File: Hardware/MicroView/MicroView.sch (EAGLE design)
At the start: 23 parts, among them J1 OLED_SCREEN, J2 MICROVIEW-16, J3 M03NS_SLIM, U1 MIC5205 3.3V, U2 SPX3819M5-L-5-0, U3 ATMEGA328P, Y1 16MHz

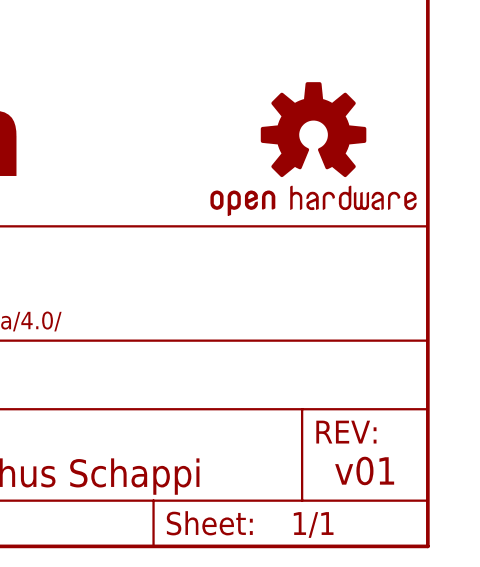
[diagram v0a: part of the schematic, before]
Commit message: Adding fids to both boards
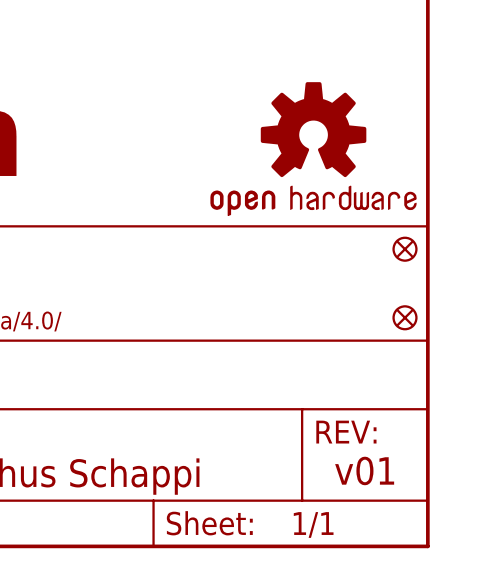
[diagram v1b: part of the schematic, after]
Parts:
- added FID1, FID3: FIDUCIAL1X2, SparkFun-Aesthetics:FIDUCIAL1X2
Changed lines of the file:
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@@
 <grid distance="0.1" unitdist="inch" unit="inch" style="lines" multiple="1" display="no" altdistance="0.01" altunitdist="inch" altunit="inch"/>
 <layers>
-<layer number="1" name="Top" color="4" fill="1" visible="no" active="no"/>
-<layer number="2" name="Route2" color="1" fill="3" visible="no" active="no"/>
-<layer number="3" name="Route3" color="4" fill="3" visible="no" active="no"/>
-<layer number="4" name="Route4" color="1" fill="4" visible="no" active="no"/>
-<layer number="5" name="Route5" color="4" fill="4" visible="no" active="no"/>
-<layer number="6" name="Route6" color="1" fill="8" visible="no" active="no"/>
-<layer number="7" name="Route7" color="4" fill="8" visible="no" active="no"/>
-<layer number="8" name="Route8" color="1" fill="2" visible="no" active="no"/>
-<layer number="9" name="Route9" color="4" fill="2" visible="no" active="no"/>
-<layer number="10" name="Route10" color="1" fill="7" visible="no" active="no"/>
-<layer number="11" name="Route11" color="4" fill="7" visible="no" active="no"/>
-<layer number="12" name="Route12" color="1" fill="5" visible="no" active="no"/>
-<layer number="13" name="Route13" color="4" fill="5" visible="no" active="no"/>
-<layer number="14" name="Route14" color="1" fill="6" visible="no" active="no"/>
-<layer number="15" name="Route15" color="4" fill="6" visible="no" active="no"/>
-<layer number="16" name="Bottom" color="1" fill="1" visible="no" active="no"/>
-<layer number="17" name="Pads" color="2" fill="1" visible="no" active="no"/>
-<layer number="18" name="Vias" color="2" fill="1" visible="no" active="no"/>
-<layer number="19" name="Unrouted" color="6" fill="1" visible="no" active="no"/>
-<layer number="20" name="Dimension" color="15" fill="1" visible="no" active="no"/>
-<layer number="21" name="tPlace" color="16" fill="1" visible="no" active="no"/>
-<layer number="22" name="bPlace" color="14" fill="1" visible="no" active="no"/>
-<layer number="23" name="tOrigins" color="15" fill="1" visible="no" active="no"/>
-<layer number="24" name="bOrigins" color="15" fill="1" visible="no" active="no"/>
-<layer number="25" name="tNames" color="7" fill="1" visible="no" active="no"/>
-<layer number="26" name="bNames" color="7" fill="1" visible="no" active="no"/>
-<layer number="27" name="tValues" color="7" fill="1" visible="no" active="no"/>
-<layer number="28" name="bValues" color="7" fill="1" visible="no" active="no"/>
+<layer number="1" name="Top" color="4" fill="1" visible="yes" active="no"/>
+<layer number="2" name="Route2" color="1" fill="3" visible="yes" active="no"/>
+<layer number="3" name="Route3" color="4" fill="3" visible="yes" active="no"/>
+<layer number="4" name="Route4" color="1" fill="4" visible="yes" active="no"/>
+<layer number="5" name="Route5" color="4" fill="4" visible="yes" active="no"/>
+<layer number="6" name="Route6" color="1" fill="8" visible="yes" active="no"/>
+<layer number="7" name="Route7" color="4" fill="8" visible="yes" active="no"/>
+<layer number="8" name="Route8" color="1" fill="2" visible="yes" active="no"/>
+<layer number="9" name="Route9" color="4" fill="2" visible="yes" active="no"/>
+<layer number="10" name="Route10" color="1" fill="7" visible="yes" active="no"/>
+<layer number="11" name="Route11" color="4" fill="7" visible="yes" active="no"/>
+<layer number="12" name="Route12" color="1" fill="5" visible="yes" active="no"/>
+<layer number="13" name="Route13" color="4" fill="5" visible="yes" active="no"/>
+<layer number="14" name="Route14" color="1" fill="6" visible="yes" active="no"/>
+<layer number="15" name="Route15" color="4" fill="6" visible="yes" active="no"/>
+<layer number="16" name="Bottom" color="1" fill="1" visible="yes" active="no"/>
+<layer number="17" name="Pads" color="2" fill="1" visible="yes" active="no"/>
+<layer number="18" name="Vias" color="2" fill="1" visible="yes" active="no"/>
+<layer number="19" name="Unrouted" color="6" fill="1" visible="yes" active="no"/>
+<layer number="20" name="Dimension" color="15" fill="1" visible="yes" active="no"/>
+<layer number="21" name="tPlace" color="16" fill="1" visible="yes" active="no"/>
+<layer number="22" name="bPlace" color="14" fill="1" visible="yes" active="no"/>
+<layer number="23" name="tOrigins" color="15" fill="1" visible="yes" active="no"/>
+<layer number="24" name="bOrigins" color="15" fill="1" visible="yes" active="no"/>
+<layer number="25" name="tNames" color="7" fill="1" visible="yes" active="no"/>
+<layer number="26" name="bNames" color="7" fill="1" visible="yes" active="no"/>
+<layer number="27" name="tValues" color="7" fill="1" visible="yes" active="no"/>
+<layer number="28" name="bValues" color="7" fill="1" visible="yes" active="no"/>
 <layer number="29" name="tStop" color="7" fill="3" visible="no" active="no"/>
 <layer number="30" name="bStop" color="7" fill="6" visible="no" active="no"/>
@@
 <layer number="35" name="tGlue" color="7" fill="4" visible="no" active="no"/>
 <layer number="36" name="bGlue" color="7" fill="5" visible="no" active="no"/>
-<layer number="37" name="tTest" color="7" fill="1" visible="no" active="no"/>
-<layer number="38" name="bTest" color="7" fill="1" visible="no" active="no"/>
+<layer number="37" name="tTest" color="7" fill="1" visible="yes" active="no"/>
+<layer number="38" name="bTest" color="7" fill="1" visible="yes" active="no"/>
 <layer number="39" name="tKeepout" color="4" fill="11" visible="no" active="no"/>
 <layer number="40" name="bKeepout" color="1" fill="11" visible="no" active="no"/>
@@
 <layer number="44" name="Drills" color="7" fill="1" visible="no" active="no"/>
 <layer number="45" name="Holes" color="7" fill="1" visible="no" active="no"/>
-<layer number="46" name="Milling" color="3" fill="1" visible="no" active="no"/>
-<layer number="47" name="Measures" color="7" fill="1" visible="no" active="no"/>
-<layer number="48" name="Document" color="7" fill="1" visible="no" active="no"/>
-<layer number="49" name="Reference" color="7" fill="1" visible="no" active="no"/>
-<layer number="50" name="dxf" color="7" fill="1" visible="no" active="no"/>
-<layer number="51" name="tDocu" color="6" fill="1" visible="no" active="no"/>
-<layer number="52" name="bDocu" color="7" fill="1" visible="no" active="no"/>
-<layer number="53" name="tGND_GNDA" color="7" fill="9" visible="no" active="no"/>
-<layer number="54" name="bGND_GNDA" color="1" fill="9" visible="no" active="no"/>
-<layer number="56" name="wert" color="7" fill="1" visible="no" active="no"/>
+<layer number="46" name="Milling" color="3" fill="1" visible="yes" active="no"/>
+<layer number="47" name="Measures" color="7" fill="1" visible="yes" active="no"/>
+<layer number="48" name="Document" color="7" fill="1" visible="yes" active="no"/>
+<layer number="49" name="Reference" color="7" fill="1" visible="yes" active="no"/>
+<layer number="50" name="dxf" color="7" fill="1" visible="yes" active="no"/>
+<layer number="51" name="tDocu" color="6" fill="1" visible="yes" active="no"/>
+<layer number="52" name="bDocu" color="7" fill="1" visible="yes" active="no"/>
+<layer number="53" name="tGND_GNDA" color="7" fill="9" visible="yes" active="no"/>
+<layer number="54" name="bGND_GNDA" color="1" fill="9" visible="yes" active="no"/>
+<layer number="56" name="wert" color="7" fill="1" visible="yes" active="no"/>
 <layer number="91" name="Nets" color="2" fill="1" visible="yes" active="yes"/>
 <layer number="92" name="Busses" color="1" fill="1" visible="yes" active="yes"/>
@@
 <part name="LOGO1" library="SparkFun-Aesthetics" deviceset="OSHW-LOGO" device="S"/>
 <part name="LOGO4" library="SparkFun-Aesthetics" deviceset="SFE_LOGO_NAME_FLAME" device=".1_INCH"/>
+<part name="FID1" library="SparkFun-Aesthetics" deviceset="FIDUCIAL" device="1X2" value="FIDUCIAL1X2"/>
+<part name="FID3" library="SparkFun-Aesthetics" deviceset="FIDUCIAL" device="1X2"/>
 </parts>
 <sheets>
@@
 <instance part="LOGO1" gate="G$1" x="236.22" y="45.72"/>
 <instance part="LOGO4" gate="G$1" x="148.082" y="36.576"/>
+<instance part="FID1" gate="G$1" x="246.38" y="33.02"/>
+<instance part="FID3" gate="G$1" x="246.38" y="25.4"/>
 </instances>
 <busses>

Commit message: Staggering/increasing drill on headers
Also spacing out resistors, increasing header fp on MicroViewUSB.
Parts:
- FID1, FID3: value FIDUCIAL1X2 -> FIDUCIALUFIDUCIAL; device SparkFun-Aesthetics:FIDUCIAL1X2 -> SparkFun-Aesthetics:FIDUCIALUFIDUCIAL
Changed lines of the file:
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@@
 <grid distance="0.1" unitdist="inch" unit="inch" style="lines" multiple="1" display="no" altdistance="0.01" altunitdist="inch" altunit="inch"/>
 <layers>
-<layer number="1" name="Top" color="4" fill="1" visible="yes" active="no"/>
-<layer number="2" name="Route2" color="1" fill="3" visible="yes" active="no"/>
-<layer number="3" name="Route3" color="4" fill="3" visible="yes" active="no"/>
-<layer number="4" name="Route4" color="1" fill="4" visible="yes" active="no"/>
-<layer number="5" name="Route5" color="4" fill="4" visible="yes" active="no"/>
-<layer number="6" name="Route6" color="1" fill="8" visible="yes" active="no"/>
-<layer number="7" name="Route7" color="4" fill="8" visible="yes" active="no"/>
-<layer number="8" name="Route8" color="1" fill="2" visible="yes" active="no"/>
-<layer number="9" name="Route9" color="4" fill="2" visible="yes" active="no"/>
-<layer number="10" name="Route10" color="1" fill="7" visible="yes" active="no"/>
-<layer number="11" name="Route11" color="4" fill="7" visible="yes" active="no"/>
-<layer number="12" name="Route12" color="1" fill="5" visible="yes" active="no"/>
-<layer number="13" name="Route13" color="4" fill="5" visible="yes" active="no"/>
-<layer number="14" name="Route14" color="1" fill="6" visible="yes" active="no"/>
-<layer number="15" name="Route15" color="4" fill="6" visible="yes" active="no"/>
-<layer number="16" name="Bottom" color="1" fill="1" visible="yes" active="no"/>
-<layer number="17" name="Pads" color="2" fill="1" visible="yes" active="no"/>
-<layer number="18" name="Vias" color="2" fill="1" visible="yes" active="no"/>
-<layer number="19" name="Unrouted" color="6" fill="1" visible="yes" active="no"/>
-<layer number="20" name="Dimension" color="15" fill="1" visible="yes" active="no"/>
-<layer number="21" name="tPlace" color="16" fill="1" visible="yes" active="no"/>
-<layer number="22" name="bPlace" color="14" fill="1" visible="yes" active="no"/>
-<layer number="23" name="tOrigins" color="15" fill="1" visible="yes" active="no"/>
-<layer number="24" name="bOrigins" color="15" fill="1" visible="yes" active="no"/>
-<layer number="25" name="tNames" color="7" fill="1" visible="yes" active="no"/>
-<layer number="26" name="bNames" color="7" fill="1" visible="yes" active="no"/>
-<layer number="27" name="tValues" color="7" fill="1" visible="yes" active="no"/>
-<layer number="28" name="bValues" color="7" fill="1" visible="yes" active="no"/>
+<layer number="1" name="Top" color="4" fill="1" visible="no" active="no"/>
+<layer number="2" name="Route2" color="1" fill="3" visible="no" active="no"/>
+<layer number="3" name="Route3" color="4" fill="3" visible="no" active="no"/>
+<layer number="4" name="Route4" color="1" fill="4" visible="no" active="no"/>
+<layer number="5" name="Route5" color="4" fill="4" visible="no" active="no"/>
+<layer number="6" name="Route6" color="1" fill="8" visible="no" active="no"/>
+<layer number="7" name="Route7" color="4" fill="8" visible="no" active="no"/>
+<layer number="8" name="Route8" color="1" fill="2" visible="no" active="no"/>
+<layer number="9" name="Route9" color="4" fill="2" visible="no" active="no"/>
+<layer number="10" name="Route10" color="1" fill="7" visible="no" active="no"/>
+<layer number="11" name="Route11" color="4" fill="7" visible="no" active="no"/>
+<layer number="12" name="Route12" color="1" fill="5" visible="no" active="no"/>
+<layer number="13" name="Route13" color="4" fill="5" visible="no" active="no"/>
+<layer number="14" name="Route14" color="1" fill="6" visible="no" active="no"/>
+<layer number="15" name="Route15" color="4" fill="6" visible="no" active="no"/>
+<layer number="16" name="Bottom" color="1" fill="1" visible="no" active="no"/>
+<layer number="17" name="Pads" color="2" fill="1" visible="no" active="no"/>
+<layer number="18" name="Vias" color="2" fill="1" visible="no" active="no"/>
+<layer number="19" name="Unrouted" color="6" fill="1" visible="no" active="no"/>
+<layer number="20" name="Dimension" color="15" fill="1" visible="no" active="no"/>
+<layer number="21" name="tPlace" color="16" fill="1" visible="no" active="no"/>
+<layer number="22" name="bPlace" color="14" fill="1" visible="no" active="no"/>
+<layer number="23" name="tOrigins" color="15" fill="1" visible="no" active="no"/>
+<layer number="24" name="bOrigins" color="15" fill="1" visible="no" active="no"/>
+<layer number="25" name="tNames" color="7" fill="1" visible="no" active="no"/>
+<layer number="26" name="bNames" color="7" fill="1" visible="no" active="no"/>
+<layer number="27" name="tValues" color="7" fill="1" visible="no" active="no"/>
+<layer number="28" name="bValues" color="7" fill="1" visible="no" active="no"/>
 <layer number="29" name="tStop" color="7" fill="3" visible="no" active="no"/>
 <layer number="30" name="bStop" color="7" fill="6" visible="no" active="no"/>
@@
 <layer number="35" name="tGlue" color="7" fill="4" visible="no" active="no"/>
 <layer number="36" name="bGlue" color="7" fill="5" visible="no" active="no"/>
-<layer number="37" name="tTest" color="7" fill="1" visible="yes" active="no"/>
-<layer number="38" name="bTest" color="7" fill="1" visible="yes" active="no"/>
+<layer number="37" name="tTest" color="7" fill="1" visible="no" active="no"/>
+<layer number="38" name="bTest" color="7" fill="1" visible="no" active="no"/>
 <layer number="39" name="tKeepout" color="4" fill="11" visible="no" active="no"/>
 <layer number="40" name="bKeepout" color="1" fill="11" visible="no" active="no"/>
@@
 <layer number="44" name="Drills" color="7" fill="1" visible="no" active="no"/>
 <layer number="45" name="Holes" color="7" fill="1" visible="no" active="no"/>
-<layer number="46" name="Milling" color="3" fill="1" visible="yes" active="no"/>
-<layer number="47" name="Measures" color="7" fill="1" visible="yes" active="no"/>
-<layer number="48" name="Document" color="7" fill="1" visible="yes" active="no"/>
-<layer number="49" name="Reference" color="7" fill="1" visible="yes" active="no"/>
-<layer number="50" name="dxf" color="7" fill="1" visible="yes" active="no"/>
-<layer number="51" name="tDocu" color="6" fill="1" visible="yes" active="no"/>
-<layer number="52" name="bDocu" color="7" fill="1" visible="yes" active="no"/>
-<layer number="53" name="tGND_GNDA" color="7" fill="9" visible="yes" active="no"/>
-<layer number="54" name="bGND_GNDA" color="1" fill="9" visible="yes" active="no"/>
-<layer number="56" name="wert" color="7" fill="1" visible="yes" active="no"/>
+<layer number="46" name="Milling" color="3" fill="1" visible="no" active="no"/>
+<layer number="47" name="Measures" color="7" fill="1" visible="no" active="no"/>
+<layer number="48" name="Document" color="7" fill="1" visible="no" active="no"/>
+<layer number="49" name="Reference" color="7" fill="1" visible="no" active="no"/>
+<layer number="50" name="dxf" color="7" fill="1" visible="no" active="no"/>
+<layer number="51" name="tDocu" color="6" fill="1" visible="no" active="no"/>
+<layer number="52" name="bDocu" color="7" fill="1" visible="no" active="no"/>
+<layer number="53" name="tGND_GNDA" color="7" fill="9" visible="no" active="no"/>
+<layer number="54" name="bGND_GNDA" color="1" fill="9" visible="no" active="no"/>
+<layer number="56" name="wert" color="7" fill="1" visible="no" active="no"/>
 <layer number="91" name="Nets" color="2" fill="1" visible="yes" active="yes"/>
 <layer number="92" name="Busses" color="1" fill="1" visible="yes" active="yes"/>
@@
 <part name="LOGO1" library="SparkFun-Aesthetics" deviceset="OSHW-LOGO" device="S"/>
 <part name="LOGO4" library="SparkFun-Aesthetics" deviceset="SFE_LOGO_NAME_FLAME" device=".1_INCH"/>
-<part name="FID1" library="SparkFun-Aesthetics" deviceset="FIDUCIAL" device="1X2" value="FIDUCIAL1X2"/>
-<part name="FID3" library="SparkFun-Aesthetics" deviceset="FIDUCIAL" device="1X2"/>
+<part name="FID1" library="SparkFun-Aesthetics" deviceset="FIDUCIAL" device="UFIDUCIAL" value="FIDUCIALUFIDUCIAL"/>
+<part name="FID3" library="SparkFun-Aesthetics" deviceset="FIDUCIAL" device="UFIDUCIAL" value="FIDUCIALUFIDUCIAL"/>
 </parts>
 <sheets>

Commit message: Microview v02 -- new resistors and 3.3Vreg change
* Added pull-down resistor to OLED Reset. Also moved that pin to D7 on
the Arduino.
* Added pull-up resistor to D10/SS.
* Moved 3.3V regulator input to the 5V line (from Vin)
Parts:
- removed J3: M03NS_SLIM, microView-temp:M03NS_SLIM
- removed Y1: 16MHz, SparkFun-FreqCtrl:RESONATOR16MHZ
- added J4: M03NS_SLIM, microView-temp:M03NS_SLIM
- added R3, R4: 10K, SparkFun-Resistors:10KOHM1/10W1%(0603)0603
- added Y2: RESONATORSMD, microView-temp:RESONATORSMD
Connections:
- new net D7/!RESET!: OLED1.!RESET!, R4.2, U3.PD7(AIN1)
- net 5V: now also C1.1, R3.2, U1.EN, U1.IN
- net D10/SS: now also R3.1
- net D11/MOSI: now also J4.1; no longer J3.1
- net D12/MISO: now also J4.3; no longer J3.2, OLED1.!RESET!
- net D13/SCK: now also J4.2; no longer J3.3
- net GND: now also R4.1, Y2.2; no longer Y1.2
- net N$8: now also Y2.1; no longer Y1.1
- net N$9: now also Y2.3; no longer Y1.3
- net VIN: no longer C1.1, U1.EN, U1.IN
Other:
- note added: "ATmega328"
- note added: "Headers"
- note added: "OLED"
- note added: "Voltage Regulators"
- moved on the sheet: C1, C2, C3, C4, U1, U2
